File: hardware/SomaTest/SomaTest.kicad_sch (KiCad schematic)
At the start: 9 parts, among them IC1 DG406DJ, J1 IN 1, J2 IN 2, J3 OUT, U1 RP2040

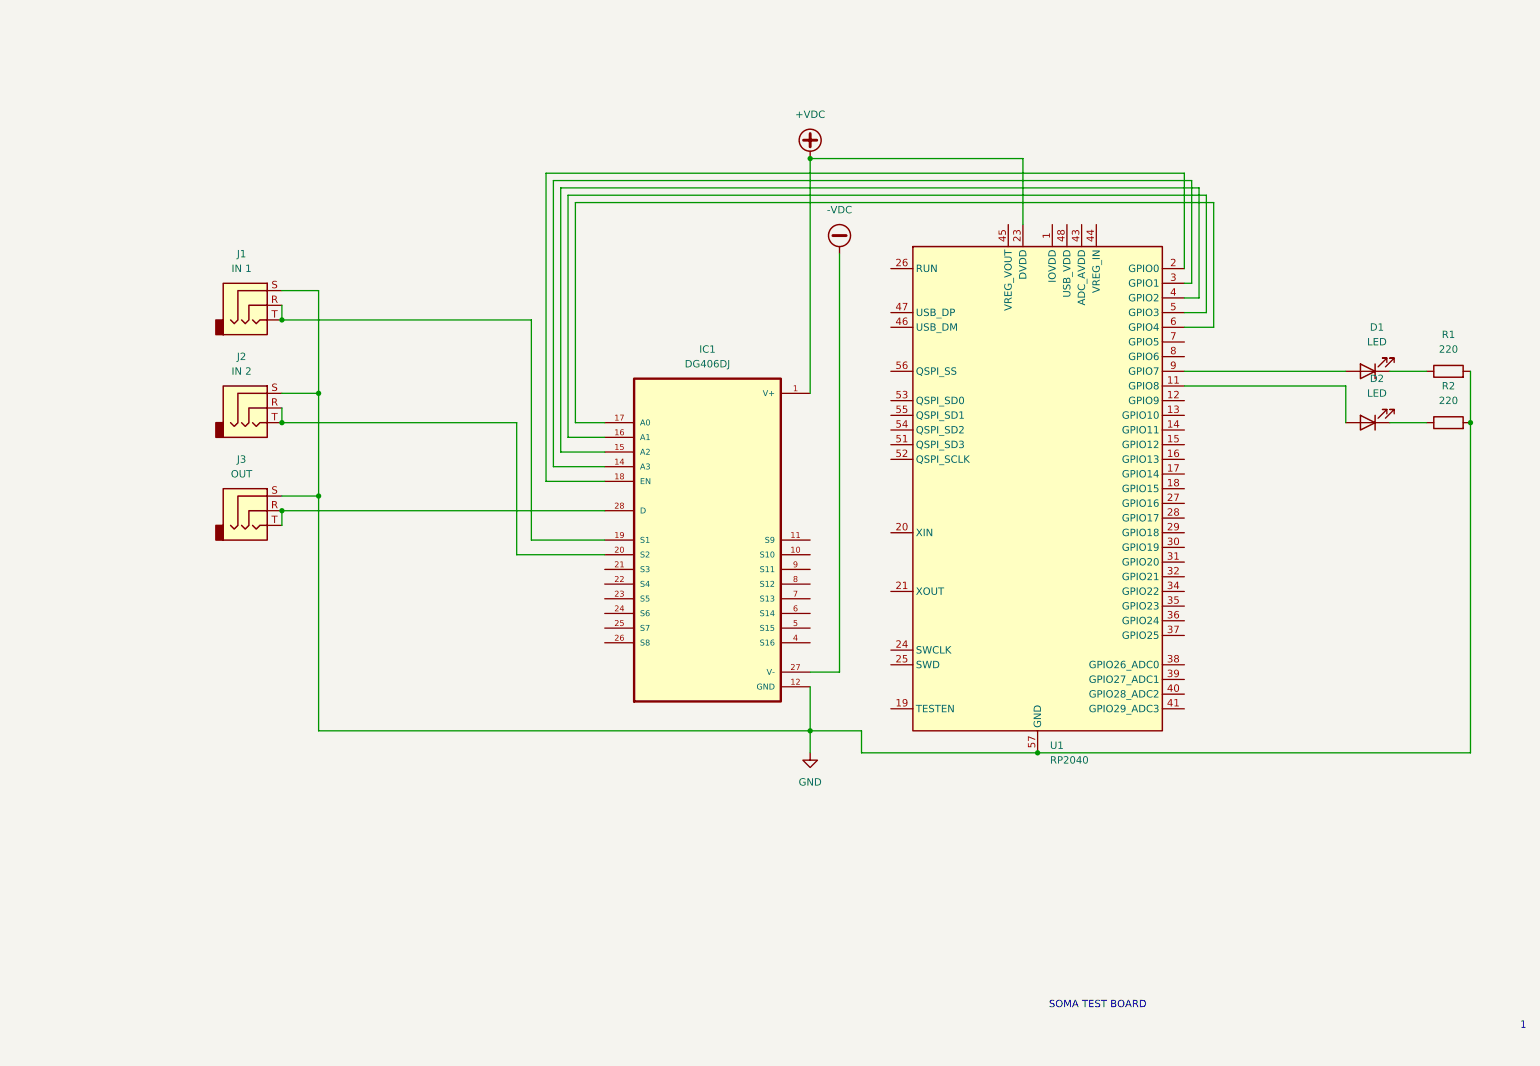
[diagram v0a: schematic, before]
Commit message: Current Design. We need to split it into two boards I think.
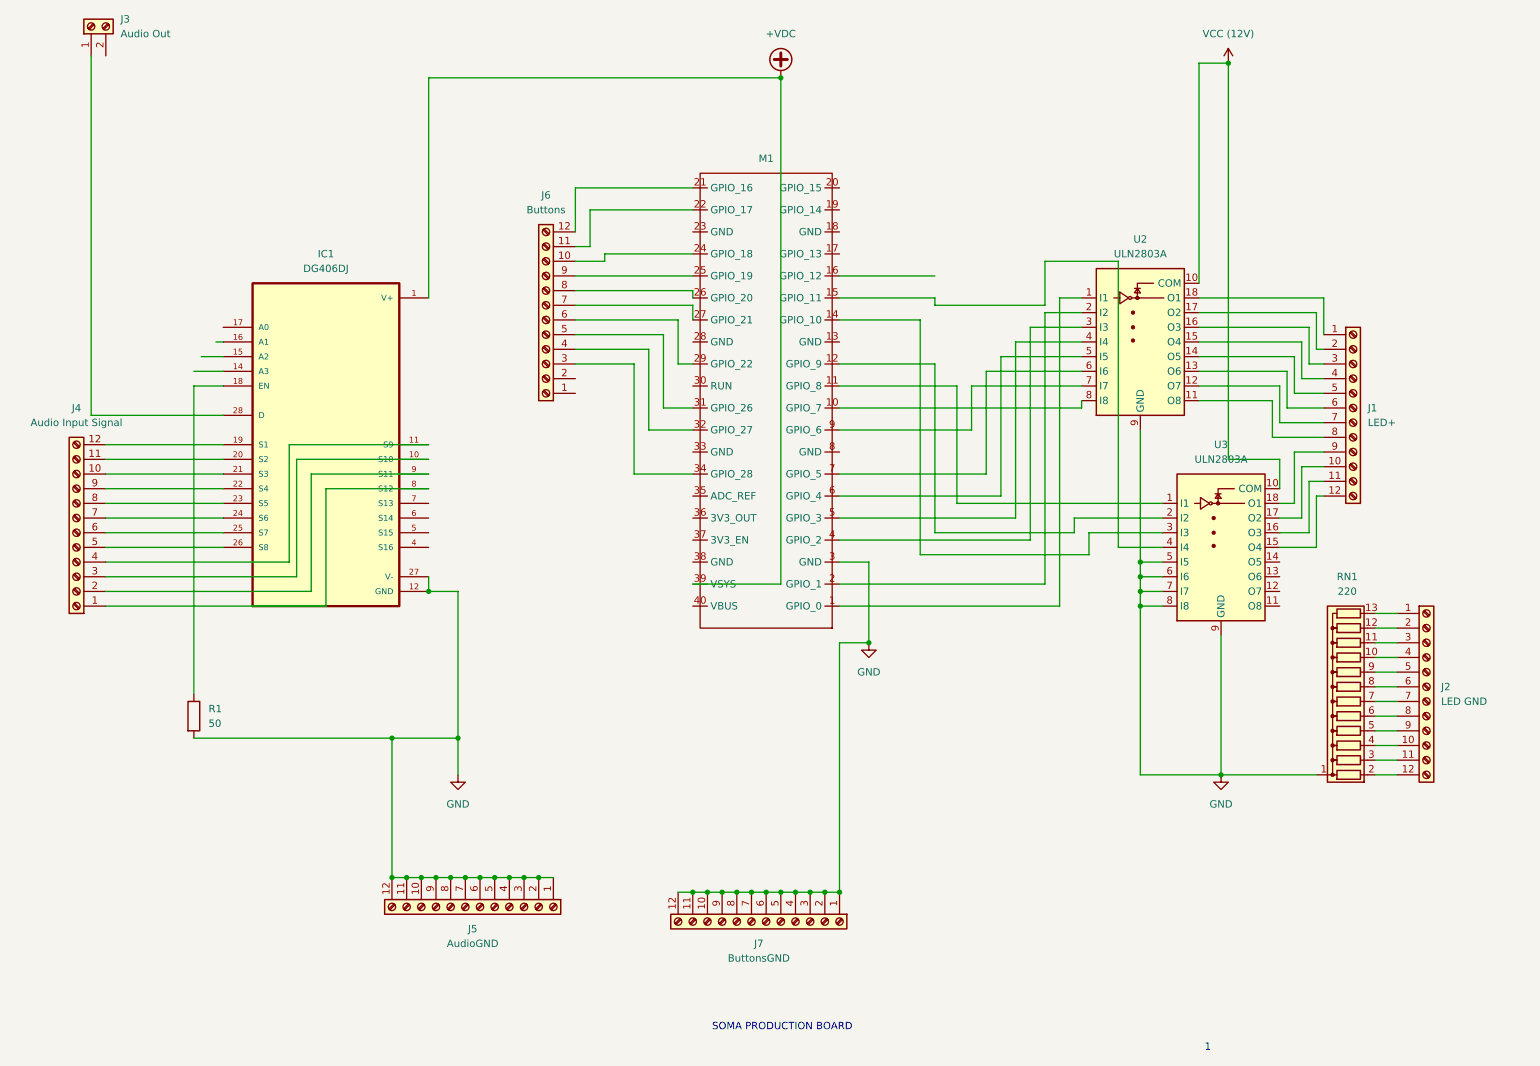
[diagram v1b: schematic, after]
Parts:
- removed D1, D2: LED, symbol Device:LED
- removed J1: IN 1, symbol Connector_Audio:AudioJack3
- removed J2: IN 2, symbol Connector_Audio:AudioJack3
- removed J3: OUT, symbol Connector_Audio:AudioJack3
- removed R2: 220, symbol Device:R
- removed U1: RP2040, Package_DFN_QFN:QFN-56-1EP_7x7mm_P0.4mm_EP3.2x3.2mm, symbol MCU_RaspberryPi:RP2040
- added J1: LED+, symbol Connector:Screw_Terminal_01x12
- added J2: LED GND, symbol Connector:Screw_Terminal_01x12
- added J3: Audio Out, symbol Connector:Screw_Terminal_01x02
- added J4: Audio Input Signal, symbol Connector:Screw_Terminal_01x12
- added J5: AudioGND, symbol Connector:Screw_Terminal_01x12
- added J6: Buttons, symbol Connector:Screw_Terminal_01x12
- added J7: ButtonsGND, symbol Connector:Screw_Terminal_01x12
- added M1: ~, symbol Pico-W Board:PicoWBoard
- added RN1: 220, Resistor_THT:R_Array_SIP13, symbol Device:R_Network12
- added U2, U3: ULN2803A, Package_SO:SOIC-18W_7.5x11.6mm_P1.27mm, symbol Transistor_Array:ULN2803A
- R1: value 220 -> 50
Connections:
- net -VDC is gone; now on net GND: IC1.27 (V-)
- net +VDC: now also M1.39 (VSYS)
- net GND: now also J5.1 (Pin_1), J5.10 (Pin_10), J5.11 (Pin_11), J5.12 (Pin_12), J5.2 (Pin_2), J5.3 (Pin_3), J5.4 (Pin_4), J5.5 (Pin_5), J5.6 (Pin_6), J5.7 (Pin_7), J5.8 (Pin_8), J5.9 (Pin_9), J7.1 (Pin_1), J7.10 (Pin_10), J7.11 (Pin_11), J7.12 (Pin_12), J7.2 (Pin_2), J7.3 (Pin_3), J7.4 (Pin_4), J7.5 (Pin_5), J7.6 (Pin_6), J7.7 (Pin_7), J7.8 (Pin_8), J7.9 (Pin_9), M1.3 (GND), RN1.1 (common), U2.9 (GND), U3.5 (I5), U3.6 (I6), U3.7 (I7), U3.8 (I8), U3.9 (GND)
- net at R1.1: now also IC1.18 (EN)
- net at IC1.10 (S10): now also J4.3 (Pin_3)
- net at IC1.11 (S9): now also J4.4 (Pin_4)
- net at IC1.19 (S1): now also J4.12 (Pin_12)
- net at IC1.20 (S2): now also J4.11 (Pin_11)
- net at IC1.21 (S3): now also J4.10 (Pin_10)
- net at IC1.22 (S4): now also J4.9 (Pin_9)
- net at IC1.23 (S5): now also J4.8 (Pin_8)
- net at IC1.24 (S6): now also J4.7 (Pin_7)
- net at IC1.25 (S7): now also J4.6 (Pin_6)
- net at IC1.26 (S8): now also J4.5 (Pin_5)
- net at IC1.28 (D): now also J3.1 (Pin_1)
- net at IC1.8 (S12): now also J4.1 (Pin_1)
- net at IC1.9 (S11): now also J4.2 (Pin_2)
- new net: M1.1 (GPIO_0), U2.1 (I1)
- new net: J1.8 (Pin_8), U2.11 (O8)
- new net: J1.7 (Pin_7), U2.12 (O7)
- new net: J1.6 (Pin_6), U2.13 (O6)
- new net: J1.5 (Pin_5), U2.14 (O5)
- new net: J1.4 (Pin_4), U2.15 (O4)
- new net: J1.3 (Pin_3), U2.16 (O3)
- new net: J1.2 (Pin_2), U2.17 (O2)
- new net: J1.1 (Pin_1), U2.18 (O1)
- new net: M1.2 (GPIO_1), U2.2 (I2)
- new net: M1.4 (GPIO_2), U2.3 (I3)
- new net: M1.5 (GPIO_3), U2.4 (I4)
- new net: M1.6 (GPIO_4), U2.5 (I5)
- new net: M1.7 (GPIO_5), U2.6 (I6)
- new net: M1.9 (GPIO_6), U2.7 (I7)
- new net: M1.10 (GPIO_7), U2.8 (I8)
- new net: J1.10 (Pin_10), U3.17 (O2)
- new net: J1.11 (Pin_11), U3.16 (O3)
- new net: J1.12 (Pin_12), U3.15 (O4)
- new net: J1.9 (Pin_9), U3.18 (O1)
- new net: M1.11 (GPIO_8), U3.1 (I1)
- new net: M1.12 (GPIO_9), U3.2 (I2)
- new net: M1.14 (GPIO_10), U3.3 (I3)
- new net: M1.15 (GPIO_11), U3.4 (I4)
- new net: J6.12 (Pin_12), M1.21 (GPIO_16)
- new net: J6.11 (Pin_11), M1.22 (GPIO_17)
- new net: J6.10 (Pin_10), M1.24 (GPIO_18)
- new net: J6.9 (Pin_9), M1.25 (GPIO_19)
- new net: J6.8 (Pin_8), M1.26 (GPIO_20)
- new net: J6.7 (Pin_7), M1.27 (GPIO_21)
- new net: J6.6 (Pin_6), M1.29 (GPIO_22)
- new net: J6.5 (Pin_5), M1.31 (GPIO_26)
- new net: J6.4 (Pin_4), M1.32 (GPIO_27)
- new net: J6.3 (Pin_3), M1.34 (GPIO_28)
- new net: J2.1 (Pin_1), RN1.13 (R12)
- new net: J2.10 (Pin_10), RN1.4 (R3)
- new net: J2.11 (Pin_11), RN1.3 (R2)
- new net: J2.12 (Pin_12), RN1.2 (R1)
- new net: J2.2 (Pin_2), RN1.12 (R11)
- new net: J2.3 (Pin_3), RN1.11 (R10)
- new net: J2.4 (Pin_4), RN1.10 (R9)
- new net: J2.5 (Pin_5), RN1.9 (R8)
- new net: J2.6 (Pin_6), RN1.8 (R7)
- new net: J2.7 (Pin_7), RN1.7 (R6)
- new net: J2.8 (Pin_8), RN1.6 (R5)
- new net: J2.9 (Pin_9), RN1.5 (R4)
- new net VCC (12V): U2.10 (COM), U3.10 (COM)
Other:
- note added: "SOMA PRODUCTION BOARD"
- note removed: "SOMA TEST BOARD"
